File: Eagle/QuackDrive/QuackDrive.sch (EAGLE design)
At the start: 101 parts, among them IC1 MCP1703T-3302E/CB, IC10 TB67H450FNG,EL, IC12 TB67H450FNG,EL, IC2 MCP1703T-3302E/CB, IC4 TB67H450FNG,EL, IC6 TB67H450FNG,EL, IC8 TB67H450FNG,EL, Q1 NPN-BJT, Q2 NPN-BJT, U1 MPU-6050-1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

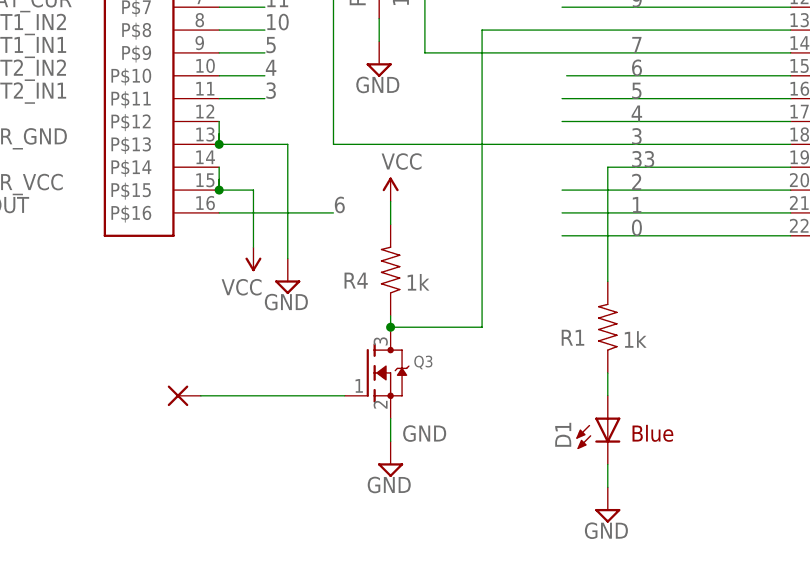
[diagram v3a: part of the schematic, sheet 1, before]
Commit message: fixed silksceeen
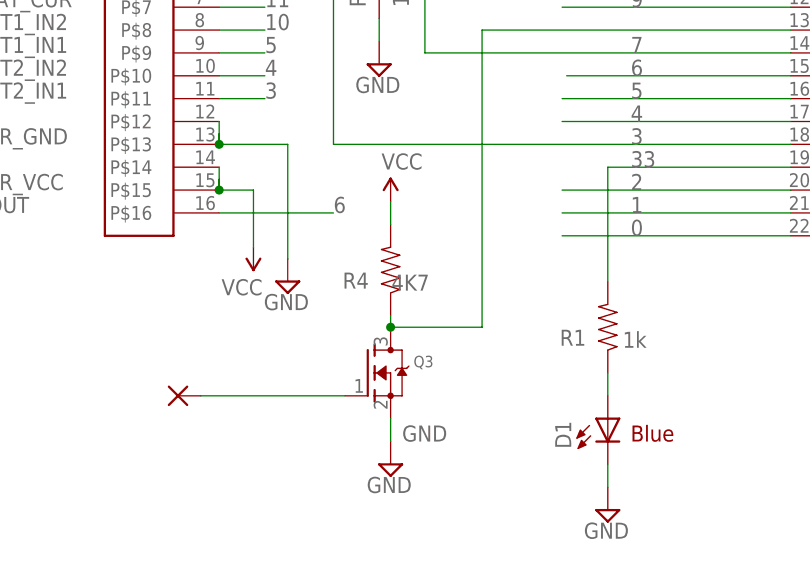
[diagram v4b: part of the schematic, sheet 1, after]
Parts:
- R4: value 1k -> 4K7
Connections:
- net N$3 renamed SBUSIN
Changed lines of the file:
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@@
 <part name="PAD23" library="wirepad" library_urn="urn:adsk.eagle:library:412" deviceset="SMD2" device="" package3d_urn="urn:adsk.eagle:package:30839/1"/>
 <part name="U3" library="ACS70331EESATR-005B3" deviceset="ACS70331EESATR-005B3" device=""/>
-<part name="R4" library="SparkFun" deviceset="RESISTOR" device="0402" value="1k"/>
+<part name="R4" library="SparkFun" deviceset="RESISTOR" device="0402" value="4K7"/>
 <part name="SUPPLY6" library="supply2" deviceset="DGND" device="" value="GND"/>
 <part name="Q3" library="adafruit" deviceset="MOSFET-N" device="REFLOW"/>
@@
 </segment>
 </net>
-<net name="N$3" class="0">
+<net name="SBUSIN" class="0">
 <segment>
 <pinref part="PAD23" gate="1" pin="P"/>
